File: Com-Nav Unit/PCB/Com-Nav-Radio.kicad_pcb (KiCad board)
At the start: 2 copper layers, 147 x 45 mm, 116 parts, among them J1 GT-USB-7055, J2 Conn_02x05_Odd_Even, J2 TC2030, J5 Conn_01x03, Q1 AO3401A, Q2 AO3401A, Q3 AO3401A, Q4 AO3401A, Q5 AO3401A, Q6 AO3401A, Q7 AO3401A, Q8 AO3401A, Q9 AO3401A, SW1 EC12E1240301, SW2 EC12D1524403, SW3 SW_Push, SW4 SW_Push, SW5 SW_Push, SW6 SW_Push, SW7 EC12D1524403, SW8 EC12E1240301, U1 FJ2352, U10 FJ2352, U11 FJ2352, U12 STM32F411CEUx, U13 74HC595, U14 74HC595, U15 74HC595, U16 74HC595, U17 ULN2003A, U18 ULN2003A, U19 ULN2003A, U2 FJ2352, U20 ULN2003A, U21 ULN2003A, U23 USBLC6-2SC6, U3 FJ2352, U4 FJ2352, U5 FJ2352, U6 FJ2352, U7 FJ2352, U8 FJ2352, U9 XC6206P332MR, Y1 25 MHz

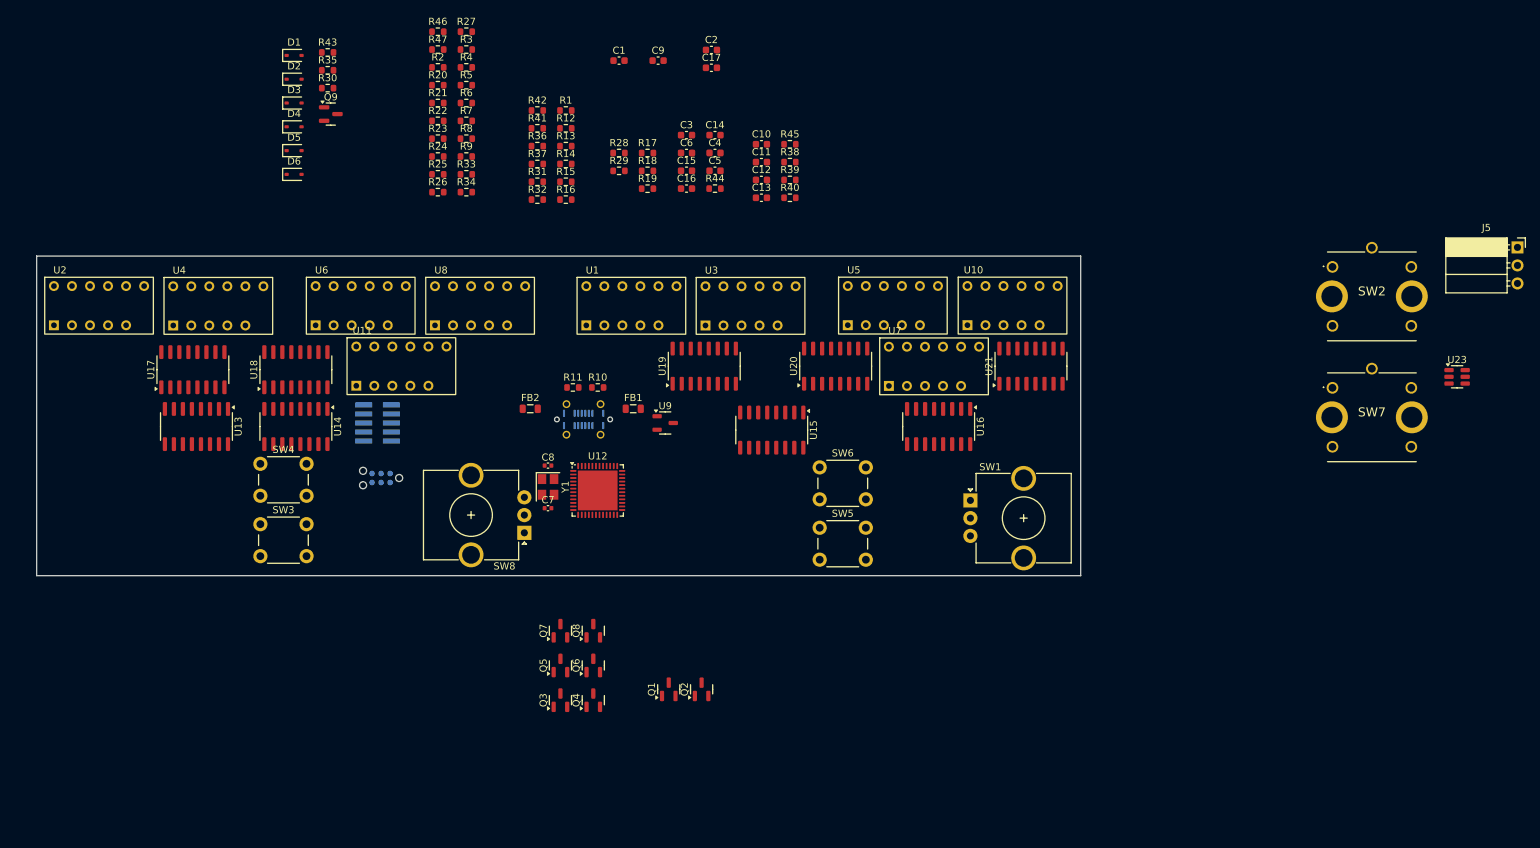
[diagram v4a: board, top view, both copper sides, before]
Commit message: PCB - work on schematic, initial board placement
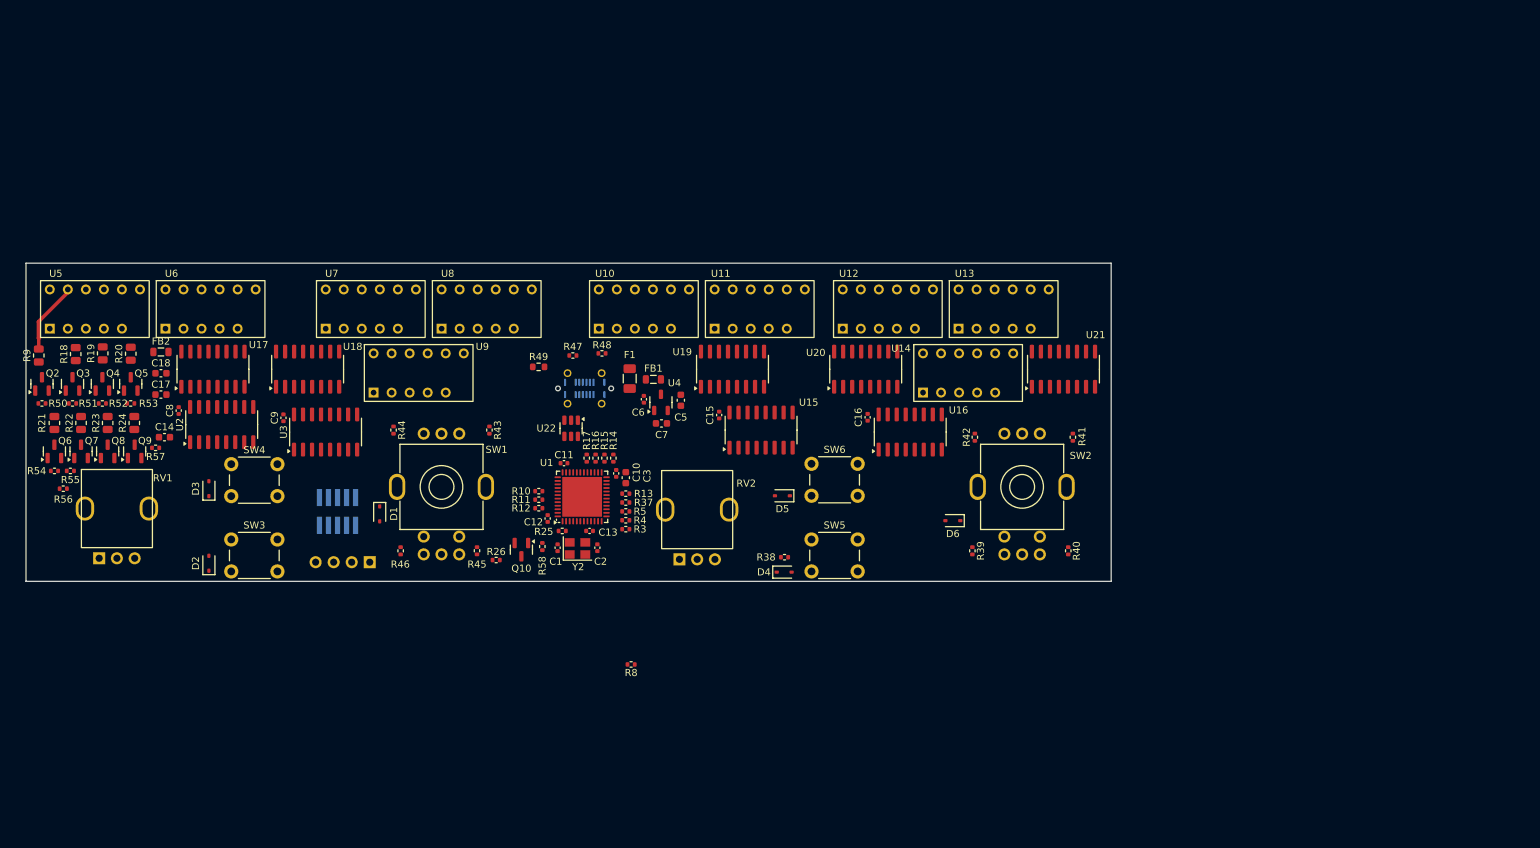
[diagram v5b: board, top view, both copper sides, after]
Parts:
- removed the C1 at (160.5, 49.5)
- removed the C2 at (173.5, 48.0)
- removed C4: 2.2u, Capacitor_SMD:C_0603_1608Metric
- removed the J2 at (127.0, 108.2)
- removed J5: Conn_01x03, Connector_PinSocket_2.54mm:PinSocket_1x03_P2.54mm_Horizontal
- removed Q1: AO3401A, Package_TO_SOT_SMD:SOT-23
- removed R1: 0, Resistor_SMD:R_0603_1608Metric
- removed R2, R27, R35, R6, R7: 100, Resistor_SMD:R_0603_1608Metric
- removed R28, R29, R30, R31, R32, R33, R34, R36: 10k, Resistor_SMD:R_0603_1608Metric
- removed the R47 at (135.0, 47.9)
- removed SW7: EC12D1524403, Encoder:EC12D1524403
- removed SW8: EC12E1240301, Encoder:EC12E1240301
- removed the U13 at (101.0, 101.0)
- removed the U14 at (115.0, 101.0)
- removed U23: USBLC6-2SC6, Package_TO_SOT_SMD:SOT-23-6
- added C18: 2.2u, Capacitor_SMD:C_0603_1608Metric, F.Cu at (96.0, 93.5)
- added C7: 2.2u, Capacitor_SMD:C_0603_1608Metric, F.Cu at (166.5, 100.6)
- added C8: 100n, Capacitor_SMD:C_0402_1005Metric, F.Cu at (98.5, 98.8)
- added F1: MF-NSMF050-2, Fuse:Fuse_1206_3216Metric, F.Cu at (162.0, 94.2)
- added J3: Conn_01x04_Pin, Connector_PinHeader_2.54mm:PinHeader_1x04_P2.54mm_Vertical, B.Cu at (125.4, 120.1)
- added Q10: AO3401A, Package_TO_SOT_SMD:SOT-23, F.Cu at (146.8, 118.3)
- added R10: 33, Resistor_SMD:R_0402_1005Metric, F.Cu at (149.2, 110.1)
- added R11: 33, Resistor_SMD:R_0402_1005Metric, F.Cu at (149.2, 111.3)
- added R49: 0, Resistor_SMD:R_0603_1608Metric, F.Cu at (149.2, 92.6)
- added R50: 10k, Resistor_SMD:R_0402_1005Metric, F.Cu at (79.2, 97.8)
- added R51: 10k, Resistor_SMD:R_0402_1005Metric, F.Cu at (83.5, 97.8)
- added R52: 10k, Resistor_SMD:R_0402_1005Metric, F.Cu at (87.8, 97.8)
- added R53: 10k, Resistor_SMD:R_0402_1005Metric, F.Cu at (91.8, 97.8)
- added R54: 10k, Resistor_SMD:R_0402_1005Metric, F.Cu at (81.0, 107.2)
- added R55: 10k, Resistor_SMD:R_0402_1005Metric, F.Cu at (83.2, 107.2)
- added R56: 10k, Resistor_SMD:R_0402_1005Metric, F.Cu at (82.2, 109.8)
- added R57: 10k, Resistor_SMD:R_0402_1005Metric, F.Cu at (95.2, 104.0)
- added R58: 10k, Resistor_SMD:R_0402_1005Metric, F.Cu at (149.7, 117.9)
- added RV1: RA0901N0X0D, Encoder:RA0901N0X0D-HA1, F.Cu at (89.8, 112.5)
- added RV2: RA0901N0X0D, Encoder:RA0901N0X0D-HA1, F.Cu at (171.5, 112.7)
- added U2: 74HC595, Package_SO:SOIC-16_3.9x9.9mm_P1.27mm, F.Cu at (104.6, 100.7)
- added U22: USBLC6-2SC6, Package_TO_SOT_SMD:SOT-23-6, F.Cu at (153.8, 101.2)
- added U3: 74HC595, Package_SO:SOIC-16_3.9x9.9mm_P1.27mm, F.Cu at (119.2, 101.8)
- C10, C11, C12, C13, C15, C16: footprint Capacitor_SMD:C_0603_1608Metric -> Capacitor_SMD:C_0402_1005Metric
- C14, C17, C3: value 100n -> 2.2u
- C6, C9: value 2.2u -> 100n; footprint Capacitor_SMD:C_0603_1608Metric -> Capacitor_SMD:C_0402_1005Metric
- D1, D2, D3, D4, D5, D6: value 1N4148WS -> 1N5819WS
- R12, R13, R14, R15, R16, R17: value 10k -> 33; footprint Resistor_SMD:R_0603_1608Metric -> Resistor_SMD:R_0402_1005Metric
- R18, R19: value 10k -> 51; footprint Resistor_SMD:R_0603_1608Metric -> Resistor_SMD:R_0805_2012Metric
- R20, R21, R22, R23, R24, R9: value 100 -> 51; footprint Resistor_SMD:R_0603_1608Metric -> Resistor_SMD:R_0805_2012Metric
- R25, R26, R3, R4, R5: value 100 -> 33; footprint Resistor_SMD:R_0603_1608Metric -> Resistor_SMD:R_0402_1005Metric
- R37, R41, R42, R43, R44, R45, R46: footprint Resistor_SMD:R_0603_1608Metric -> Resistor_SMD:R_0402_1005Metric
- R38, R39, R40, R8: value 100 -> 10k; footprint Resistor_SMD:R_0603_1608Metric -> Resistor_SMD:R_0402_1005Metric
- R47: renamed from R11; footprint Resistor_SMD:R_0603_1608Metric -> Resistor_SMD:R_0402_1005Metric
- R48: renamed from R10; footprint Resistor_SMD:R_0603_1608Metric -> Resistor_SMD:R_0402_1005Metric
- SW1: value EC12E1240301 -> EC110701N2B; footprint Encoder:EC12E1240301 -> Encoder:EC11EBB24C03_EC110701N2B
- SW2: value EC12D1524403 -> EC110701N2B; footprint Encoder:EC12D1524403 -> Encoder:EC11EBB24C03_EC110701N2B
- moved D6 104.8 mm to (207.5, 114.2), turned to 180 degrees
- moved Q2 102.3 mm to (79.2, 95.0)
- moved D4 93.2 mm to (183.8, 121.5)
- moved C17 90.1 mm to (96.0, 96.5)
- moved C14 88.4 mm to (96.5, 102.5)
- moved R41 87.0 mm to (224.4, 102.5), turned to 90 degrees
- moved R18 84.5 mm to (84.0, 90.8), turned to 90 degrees
- moved D5 84.2 mm to (183.5, 110.8), turned to 180 degrees
- moved Q4 82.2 mm to (87.8, 95.0)
- moved Q3 81.9 mm to (83.5, 95.0)
- moved Q6 81.6 mm to (81.0, 104.5)
- moved R19 80.1 mm to (87.8, 90.7), turned to 90 degrees
- moved R8 77.6 mm to (162.2, 134.5), turned to 180 degrees
- moved R42 76.9 mm to (210.6, 102.5), turned to 90 degrees
- moved SW1 74.5 mm to (135.5, 109.5), turned to 180 degrees
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- renumbered C8 to C1, C7 to C2, U12 to U1, U1 to U10, U3 to U11, U5 to U12, U10 to U13, U7 to U14, U9 to U4, U2 to U5, U4 to U6, U6 to U7, U11 to U9, Y1 to Y2
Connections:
- C1 pad 1: Net-(U12-PH1) -> Net-(U1-PH1)
- C1 pad 2: Net-(C7-Pad2) -> GND
- C14 pad 1: +3.3V -> Net-(Q2-S)
- C17 pad 1: +3.3V -> Net-(Q2-S)
- C2 pad 1: Net-(U12-PH0) -> Net-(U1-PH0)
- C2 pad 2: Net-(C7-Pad2) -> GND
- C3 pad 1: unconnected-(C3-Pad1) -> Net-(U1-VCAP1)
- C3 pad 2: unconnected-(C3-Pad2) -> GND
- C5 pad 1: Net-(C5-Pad1) -> Net-(U4-VI)
- C5 pad 2: Net-(C2-Pad2) -> GND
- C6 pad 1: +3.3V -> Net-(U4-VI)
- C6 pad 2: Net-(C1-Pad2) -> GND
- C9 pad 1: Net-(U12-VCAP1) -> +3.3V
- D1 pad 1: Net-(D1-K) -> /DIG1
- D1 pad 2: /DIG1 -> Net-(D1-A)
- D2 pad 1: Net-(D2-K) -> /DIG2
- D2 pad 2: /DIG2 -> Net-(D2-A)
- D3 pad 1: Net-(D3-K) -> /DIG3
- D3 pad 2: /DIG3 -> Net-(D3-A)
- D4 pad 1: Net-(D4-K) -> /DIG4
- D4 pad 2: /DIG4 -> /BOOT0
- D5 pad 1: Net-(D5-K) -> /DIG5
- D5 pad 2: /DIG5 -> Net-(D5-A)
- D6 pad 1: Net-(D6-K) -> /DIG6
- D6 pad 2: /DIG6 -> Net-(D6-A)
- FB1 pad 1: Net-(U23-VBUS) -> Net-(U22-VBUS)
- FB1 pad 2: Net-(U9-VI) -> Net-(U4-VI)
- FB2 pad 1: unconnected-(FB2-Pad1) -> Net-(U22-VBUS)
- FB2 pad 2: Net-(C5-Pad1) -> Net-(Q2-S)
- J1 pad A4: Net-(U23-VBUS) -> Net-(F1-Pad1)
- J1 pad A9: Net-(U23-VBUS) -> Net-(F1-Pad1)
- J1 pad B4: Net-(U23-VBUS) -> Net-(F1-Pad1)
- J1 pad B9: Net-(U23-VBUS) -> Net-(F1-Pad1)
- J2 pad 1: +3V3 -> +3.3V
- Q2 pad 2: unconnected-(Q2-S-Pad2) -> Net-(Q2-S)
- Q3 pad 2: unconnected-(Q3-S-Pad2) -> Net-(Q2-S)
- Q4 pad 2: unconnected-(Q4-S-Pad2) -> Net-(Q2-S)
- Q5 pad 2: unconnected-(Q5-S-Pad2) -> Net-(Q2-S)
- Q6 pad 2: unconnected-(Q6-S-Pad2) -> Net-(Q2-S)
- Q7 pad 2: unconnected-(Q7-S-Pad2) -> Net-(Q2-S)
- Q8 pad 2: unconnected-(Q8-S-Pad2) -> Net-(Q2-S)
- Q9 pad 2: +3.3V -> Net-(Q2-S)
- Q9 pad 3: unconnected-(Q9-D-Pad3) -> Net-(Q9-D)
- R12 pad 1: unconnected-(R12-Pad1) -> /SEG_CT3
- R12 pad 2: unconnected-(R12-Pad2) -> Net-(Q4-G)
- R13 pad 1: unconnected-(R13-Pad1) -> /SEG_CT4
- R13 pad 2: unconnected-(R13-Pad2) -> Net-(Q5-G)
- R14 pad 1: unconnected-(R14-Pad1) -> /SEG_CT5
- R14 pad 2: unconnected-(R14-Pad2) -> Net-(Q6-G)
- R15 pad 1: unconnected-(R15-Pad1) -> /SEG_CT6
- R15 pad 2: unconnected-(R15-Pad2) -> Net-(Q7-G)
- R16 pad 1: unconnected-(R16-Pad1) -> /SEG_CT7
- R16 pad 2: unconnected-(R16-Pad2) -> Net-(Q8-G)
- R17 pad 1: unconnected-(R17-Pad1) -> /SEG_CT8
- R17 pad 2: unconnected-(R17-Pad2) -> Net-(Q9-G)
- R18 pad 1: unconnected-(R18-Pad1) -> Net-(Q3-D)
- R18 pad 2: unconnected-(R18-Pad2) -> /SEG2
- R19 pad 1: unconnected-(R19-Pad1) -> Net-(Q4-D)
- R19 pad 2: unconnected-(R19-Pad2) -> /SEG3
- R20 pad 1: /SEG_CT1 -> Net-(Q5-D)
- R20 pad 2: Net-(Q1-G) -> /SEG4
- R21 pad 1: /SEG_CT2 -> Net-(Q6-D)
- R21 pad 2: Net-(Q2-G) -> /SEG5
- R22 pad 1: /SEG_CT3 -> Net-(Q7-D)
- R22 pad 2: Net-(Q3-G) -> /SEG6
- R23 pad 1: /SEG_CT4 -> Net-(Q8-D)
- R23 pad 2: Net-(Q4-G) -> /SEG7
- R24 pad 1: /SEG_CT5 -> Net-(Q9-D)
- R24 pad 2: Net-(Q5-G) -> /SEG8
- R25 pad 1: /SEG_CT6 -> Net-(U1-PC13)
- R25 pad 2: Net-(Q6-G) -> /BOOT0_DIS
- R26 pad 1: /SEG_CT7 -> Net-(D2-A)
- R26 pad 2: Net-(Q7-G) -> Net-(Q10-D)
- R3 pad 1: Net-(Q2-D) -> Net-(U2-SER)
- R3 pad 2: /SEG2 -> Net-(U1-PA2)
- R37 pad 1: Net-(R36-Pad1) -> GND
- R37 pad 2: /ENC1_B -> Net-(U1-PB2)
- R38 pad 1: Net-(U13-SER) -> GND
- R38 pad 2: Net-(U12-PA2) -> /BOOT0
- R39 pad 1: unconnected-(R39-Pad1) -> +3.3V
- R39 pad 2: Net-(U12-PA3) -> /ENC2_B
- R4 pad 1: Net-(Q3-D) -> Net-(U15-~{OE})
- R4 pad 2: /SEG3 -> Net-(U1-PA3)
- R40 pad 1: Net-(U16-RCLK) -> +3.3V
- R40 pad 2: Net-(U12-PA5) -> /ENC2_A
- R41 pad 1: Net-(R41-Pad1) -> +3.3V
- R41 pad 2: /ENC2_A -> /ENC1_A
- R42 pad 1: Net-(R41-Pad1) -> +3.3V
- R42 pad 2: /ENC2_B -> /ENC1_B
- R43 pad 1: Net-(U16-~{OE}) -> +3.3V
- R43 pad 2: +3.3V -> /ENC3_A
- R44 pad 1: Net-(U13-~{SRCLR}) -> +3.3V
- R44 pad 2: +3.3V -> /ENC3_B
- R45 pad 1: Net-(U14-~{SRCLR}) -> +3.3V
- R45 pad 2: +3.3V -> /ENC4_A
- R46 pad 1: Net-(U15-~{SRCLR}) -> +3.3V
- R46 pad 2: +3.3V -> /ENC4_B
- R47 pad 2: Net-(R10-Pad2) -> GND
- R48 pad 2: Net-(R10-Pad2) -> GND
- R5 pad 1: Net-(Q4-D) -> Net-(U15-RCLK)
- R5 pad 2: /SEG4 -> Net-(U1-PA5)
- R8 pad 1: Net-(Q7-D) -> Net-(U15-~{OE})
- R8 pad 2: /SEG7 -> +3.3V
- R9 pad 1: Net-(Q8-D) -> Net-(Q2-D)
- R9 pad 2: /SEG8 -> /SEG1
- SW3 pad 1: unconnected-(SW3-Pad1) -> /SW_COM
- SW3 pad 2: Net-(D2-K) -> Net-(D2-A)
- SW4 pad 1: unconnected-(SW4-Pad1) -> /SW_COM
- SW4 pad 2: Net-(D3-K) -> Net-(D3-A)
- SW5 pad 2: Net-(D4-K) -> /BOOT0
- SW6 pad 1: unconnected-(SW6-Pad1) -> /SW_COM
- SW6 pad 2: Net-(D5-K) -> Net-(D5-A)
- U1 pad 12: Net-(U12-PA2) -> Net-(U1-PA2)
- U1 pad 13: Net-(U12-PA3) -> Net-(U1-PA3)
- U1 pad 15: Net-(U12-PA5) -> Net-(U1-PA5)
- U1 pad 16: unconnected-(U12-PA6-Pad16) -> /POT2
- U1 pad 2: Net-(U12-PC13) -> Net-(U1-PC13)
- U1 pad 20: Net-(U12-PB2) -> Net-(U1-PB2)
- U1 pad 22: Net-(U12-VCAP1) -> Net-(U1-VCAP1)
- U1 pad 23: Net-(U12-VSSA) -> GND
- U1 pad 24: Net-(U12-VDDA) -> +3.3V
- U1 pad 32: /USB_D- -> /USB_DN
- U1 pad 33: /USB_D+ -> /USB_DP
- U1 pad 35: Net-(U12-VSSA) -> GND
- U1 pad 44: Net-(U12-BOOT0) -> /BOOT0
- U1 pad 47: Net-(U12-VSSA) -> GND
- U1 pad 48: unconnected-(U12-VDD-Pad48) -> +3.3V
- U1 pad 49: Net-(U12-VSSA) -> GND
- U1 pad 5: Net-(U12-PH0) -> Net-(U1-PH0)
- U1 pad 6: Net-(U12-PH1) -> Net-(U1-PH1)
- U1 pad 8: Net-(U12-VSSA) -> GND
- U1 pad 9: Net-(U12-VDDA) -> +3.3V
- U15 pad 10: Net-(U15-~{SRCLR}) -> +3.3V
- U15 pad 11: unconnected-(U15-SRCLK-Pad11) -> Net-(U15-RCLK)
- U15 pad 12: unconnected-(U15-RCLK-Pad12) -> Net-(U15-RCLK)
- U15 pad 13: unconnected-(U15-~{OE}-Pad13) -> Net-(U15-~{OE})
- U16 pad 10: Net-(U16-~{SRCLR}) -> +3.3V
- U16 pad 11: unconnected-(U16-SRCLK-Pad11) -> Net-(U15-RCLK)
- U16 pad 12: Net-(U16-RCLK) -> Net-(U15-RCLK)
- U16 pad 13: Net-(U16-~{OE}) -> Net-(U15-~{OE})
- U21 pad 4: unconnected-(U21-I4-Pad4) -> GND
- U21 pad 5: unconnected-(U21-I5-Pad5) -> GND
- U21 pad 6: unconnected-(U21-I6-Pad6) -> GND
- U21 pad 7: unconnected-(U21-I7-Pad7) -> GND
- U4 pad 3: Net-(U9-VI) -> Net-(U4-VI)
- Y2 pad 1: unconnected-(Y1-Pad1) -> Net-(U1-PH0)
- Y2 pad 2: unconnected-(Y1-Pad2) -> GND
- Y2 pad 3: unconnected-(Y1-Pad3) -> Net-(U1-PH1)
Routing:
- net /SEG1: track 0.00 -> 10.1 mm
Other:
- board size 147 x 45 mm -> 152.8 x 44.8 mm

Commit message: PCB - Sketch routing of the 7 segments
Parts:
- moved FB2 65.6 mm to (160.8, 100.5)
- moved C18 20.5 mm to (98.7, 113.8)
- moved C17 19.4 mm to (98.7, 115.7)
- moved C14 15.5 mm to (98.7, 117.8)
- moved R56 15.3 mm to (92.0, 97.9), turned to 0 degrees
- moved Q3 14.5 mm to (94.4, 104.6)
- moved R18 14.1 mm to (94.3, 100.5)
- moved R51 13.1 mm to (81.9, 110.7)
- moved R50 10.1 mm to (79.4, 107.8)
- moved R23 10.0 mm to (92.0, 91.1)
- moved Q8 9.94 mm to (92.0, 95.2)
- moved Q6 9.63 mm to (79.5, 95.0)
- moved R54 9.55 mm to (79.6, 97.8)
- moved R21 9.52 mm to (79.5, 91.1)
- moved Q2 9.51 mm to (81.2, 104.3)
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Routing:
- net /SEG8: track 0.00 -> 40.3 mm
- net /DIG15: track 0.00 -> 37.2 mm
- net /DIG12: track 0.00 -> 34.1 mm
- net /DIG11: track 0.00 -> 32.1 mm
- net /SEG7: track 0.00 -> 30.7 mm
- net /SEG3: track 0.00 -> 29.6 mm
- net /SEG4: track 0.00 -> 28.8 mm
- net /SEG5: track 0.00 -> 28.1 mm
- net /SEG2: track 0.00 -> 26.0 mm
- net /DIG10: track 0.00 -> 25.9 mm
- net /SEG6: track 0.00 -> 25.2 mm
- net /DIG1: track 0.00 -> 23.8 mm
- net /DIG7: track 0.00 -> 22.3 mm
- net /DIG27: track 0.00 -> 22.0 mm
- net /DIG9: track 0.00 -> 21.3 mm
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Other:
- copper layers 2 -> 4
